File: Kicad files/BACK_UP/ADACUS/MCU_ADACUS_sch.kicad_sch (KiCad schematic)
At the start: 41 parts, among them J200 USB_C_Receptacle_USB2.0_14P, U200 STM32F103CBT6, U201 USBLC6-2SC6, Y200 16MHz

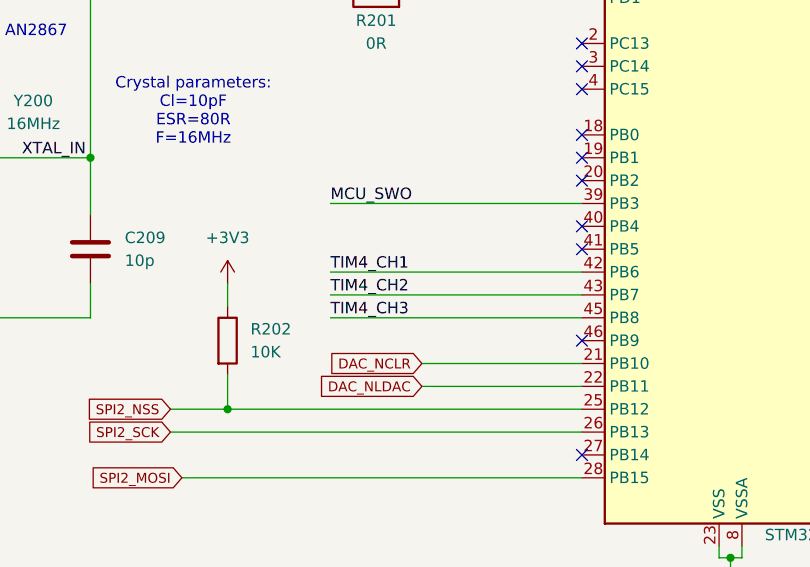
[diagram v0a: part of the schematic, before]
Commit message: [FILE] Finished board
Added PCB documents and finished schematics. Project is now done with both Altium and Kicad files uploaded
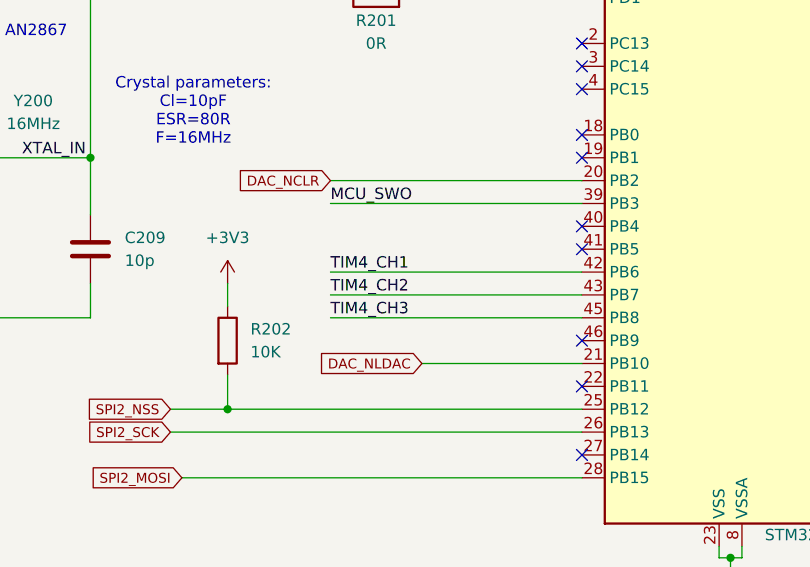
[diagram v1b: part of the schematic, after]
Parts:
- D201, D202, D203, D204, D205: value PESD3V3L1UB,115 -> PESD3V3L1UB,115
- J200: footprint Connector_USB:USB_C_Receptacle_GCT_USB4105-xx-A_16P_TopMnt_Horizontal -> Connector_USB:USB_C_Receptacle_HRO_TYPE-C-31-M-12
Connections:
- net DAC_NCLR: now also U200.20 (PB2); no longer U200.21 (PB10)
- net DAC_NLDAC: now also U200.21 (PB10); no longer U200.22 (PB11)
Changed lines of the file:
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@@
 	)
 	(no_connect
-		(at 104.14 92.71)
+		(at 104.14 115.57)
 	)
 	(no_connect
@@
 	(wire
 		(pts
+			(xy 86.36 113.03) (xy 104.14 113.03)
+		)
+		(stroke
+			(width 0)
+			(type default)
+		)
+	)
+	(wire
+		(pts
 			(xy 91.44 187.96) (xy 91.44 190.5)
 		)
@@
 	(wire
 		(pts
+			(xy 104.14 92.71) (xy 76.2 92.71)
+		)
+		(stroke
+			(width 0)
+			(type default)
+		)
+	)
+	(wire
+		(pts
 			(xy 119.38 134.62) (xy 120.65 134.62)
 		)
@@
 	(wire
 		(pts
-			(xy 86.36 115.57) (xy 104.14 115.57)
-		)
-		(stroke
-			(width 0)
-			(type default)
-		)
-	)
-	(wire
-		(pts
 			(xy 52.07 44.45) (xy 64.77 44.45)
 		)
@@
 	(wire
 		(pts
-			(xy 86.36 113.03) (xy 104.14 113.03)
-		)
-		(stroke
-			(width 0)
-			(type default)
-		)
-	)
-	(wire
-		(pts
 			(xy 115.57 172.72) (xy 143.51 172.72)
 		)
@@
 	(global_label "DAC_NLDAC"
 		(shape input)
-		(at 86.36 115.57 180)
+		(at 86.36 113.03 180)
 		(fields_autoplaced yes)
 		(effects
@@
 		)
 		(property "Intersheetrefs" "${INTERSHEET_REFS}"
-			(at 74.6079 115.57 0)
+			(at 74.6079 113.03 0)
 			(effects
 				(font
@@
 	(global_label "DAC_NCLR"
 		(shape input)
-		(at 86.36 113.03 180)
+		(at 76.2 92.71 180)
 		(fields_autoplaced yes)
 		(effects
@@
 		)
 		(property "Intersheetrefs" "${INTERSHEET_REFS}"
-			(at 75.5508 113.03 0)
+			(at 65.3908 92.71 0)
 			(effects
 				(font
@@
 			)
 		)
-		(property "Value" "PESD3V3L1UB,115 "
+		(property "Value" "PESD3V3L1UB,115"
 			(at 30.48 181.61 90)
 			(effects
@@
 			)
 		)
-		(property "Value" "PESD3V3L1UB,115 "
+		(property "Value" "PESD3V3L1UB,115"
 			(at 71.12 193.04 90)
 			(effects
@@
 			)
 		)
-		(property "Value" "PESD3V3L1UB,115 "
+		(property "Value" "PESD3V3L1UB,115"
 			(at 59.69 193.04 90)
 			(effects
@@
 			)
 		)
-		(property "Value" "PESD3V3L1UB,115 "
+		(property "Value" "PESD3V3L1UB,115"
 			(at 82.55 193.04 90)
 			(effects
@@
 			)
 		)
-		(property "Value" "PESD3V3L1UB,115 "
+		(property "Value" "PESD3V3L1UB,115"
 			(at 105.41 186.69 90)
 			(effects
@@
 			)
 		)
-		(property "Footprint" "Connector_USB:USB_C_Receptacle_GCT_USB4105-xx-A_16P_TopMnt_Horizontal"
+		(property "Footprint" "Connector_USB:USB_C_Receptacle_HRO_TYPE-C-31-M-12"
 			(at 260.35 102.87 0)
 			(effects
